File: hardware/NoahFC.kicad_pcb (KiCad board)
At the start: 2 copper layers, 32 x 42 mm, 52 parts, among them J1 ALE, J10 ESC-, J11 CAM, J12 VTX, J15 ESC_PWM, J17 BEC, J2 ELE, J3 VCC, J4 FTDI, J5 GND, J6 THR, J7 PPM, J8 GPS, J9 ESC+, U1 ATmega328, U3 XC6206, U4 LM317, U6 AT7456, Y1 16Mhz, Y3 27Mhz

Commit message: add rev10
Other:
- board text added: "NoahFC rev10"
- board text removed: "NoahFC rev9"
- board text removed: "http://github.com/zosko/NoahFC by Bosko"

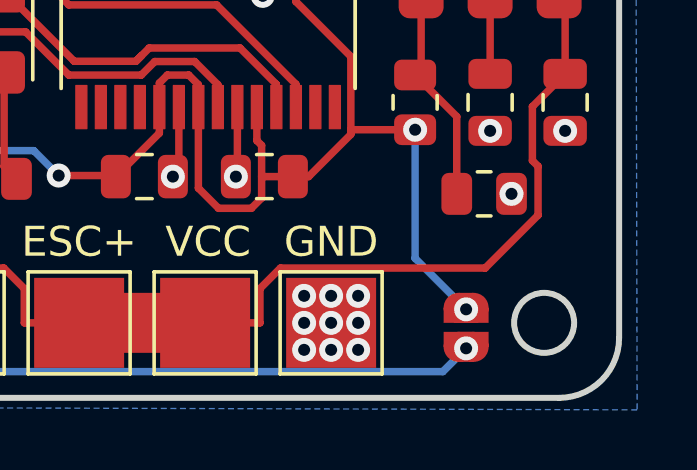
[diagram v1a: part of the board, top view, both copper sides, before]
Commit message: more space for 5v - bec
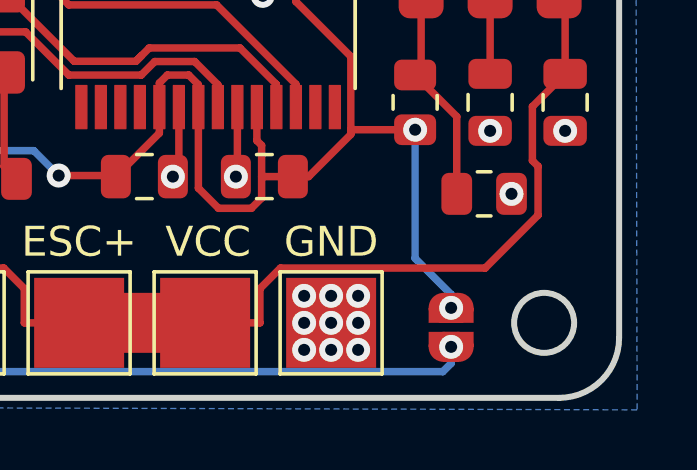
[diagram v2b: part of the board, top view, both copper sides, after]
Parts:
- moved JP2 0.50 mm to (88.6, 112.8)
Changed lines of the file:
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@@
 	(footprint "Jumper:SolderJumper-2_P1.3mm_Open_RoundedPad1.0x1.5mm"
 		(layer "F.Cu")
-		(at 89.1 112.85 90)
+		(at 88.6 112.85 90)
 		(descr "SMD Solder Jumper, 1x1.5mm, rounded Pads, 0.3mm gap, open")
 		(tags "solder jumper open")
@@
 	)
 	(via
-		(at 89.1 113.55)
+		(at 88.6 113.5)
 		(size 0.8)
 		(drill 0.4)
@@
 	)
 	(segment
+		(start 68.026 114.326)
+		(end 88.324 114.326)
+		(width 0.25)
+		(layer "B.Cu")
+		(net "BEC_5V")
+	)
+	(segment
 		(start 67.774 114.326)
 		(end 63.826 114.326)
@@
 	)
 	(segment
+		(start 67.9 114.452)
+		(end 68.026 114.326)
+		(width 0.25)
+		(layer "B.Cu")
+		(net "BEC_5V")
+	)
+	(segment
 		(start 88.324 114.326)
-		(end 89.1 113.55)
+		(end 88.6 114.05)
 		(width 0.25)
 		(layer "B.Cu")
@@
 	)
 	(segment
-		(start 68.026 114.326)
-		(end 88.324 114.326)
+		(start 88.6 114.05)
+		(end 88.6 113.5)
 		(width 0.25)
 		(layer "B.Cu")
@@
 	)
 	(segment
-		(start 67.9 114.452)
-		(end 68.026 114.326)
-		(width 0.25)
-		(layer "B.Cu")
-		(net "BEC_5V")
-	)
-	(segment
 		(start 75.4564 88.4616)
 		(end 75.8706 88.0474)
@@
 	)
 	(via
-		(at 89.1 112.25)
+		(at 88.6 112.2)
 		(size 0.8)
 		(drill 0.4)
@@
 	)
 	(segment
-		(start 74.6891 106.96)
-		(end 75.5186 107.7895)
+		(start 87.4 110.55)
+		(end 88.6 111.75)
 		(width 0.25)
 		(layer "B.Cu")
@@
 	)
 	(segment
-		(start 87.4 110.55)
-		(end 89.1 112.25)
+		(start 74.6891 106.96)
+		(end 75.5186 107.7895)
 		(width 0.25)
 		(layer "B.Cu")
@@
 		(width 0.25)
 		(layer "B.Cu")
+		(net "5V")
+	)
+	(segment
+		(start 88.6 111.75)
+		(end 88.6 112.3)
+		(width 0.25)
+		(layer "B.Cu")
